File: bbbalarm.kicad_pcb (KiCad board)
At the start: 2 copper layers, 54.6 x 86.4 mm, 34 parts, among them J101 IN0, J102 PWR, J103 IN1, J104 PIR0, J105 PIR1, P8 BeagleBone_Black_Header, P9 BeagleBone_Black_Header, SW101 Reset, SW102 PWR, U101 HCPL-263N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

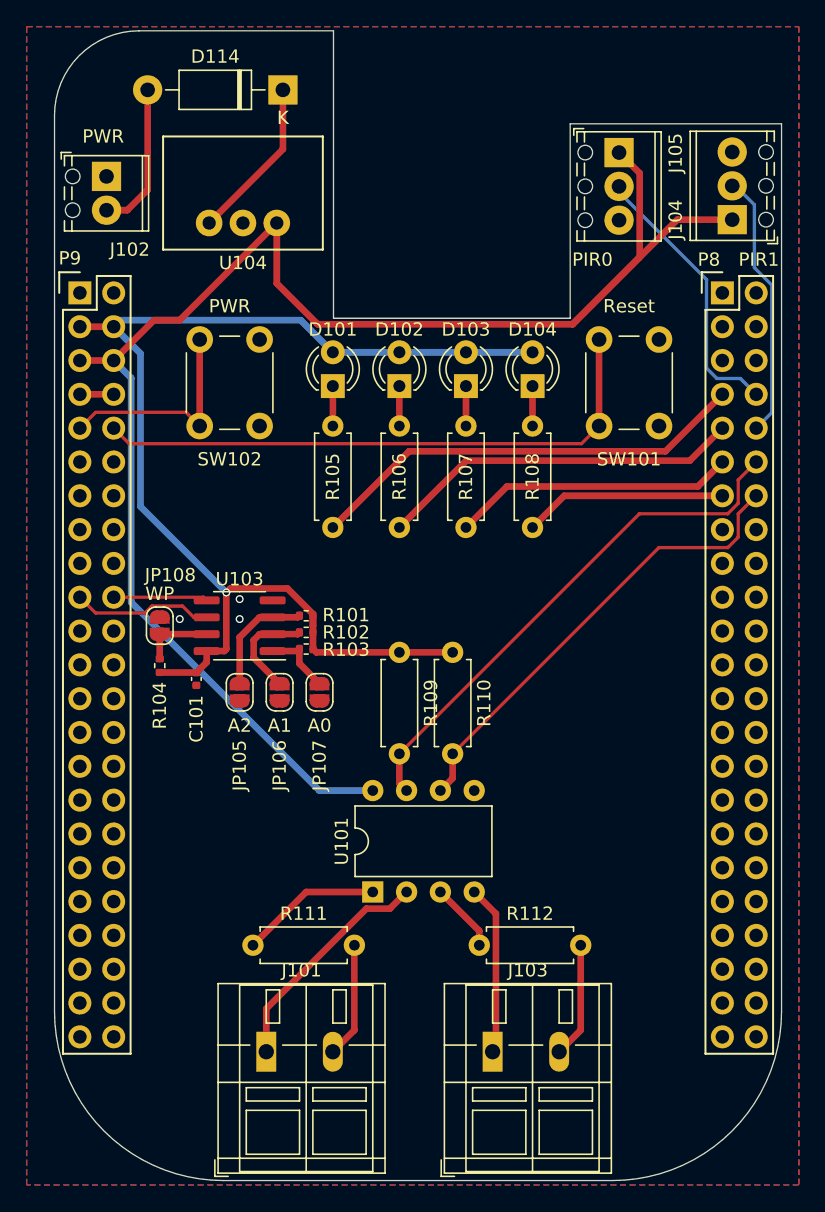
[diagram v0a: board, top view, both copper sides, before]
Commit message: Update to KiCAD v6
Signed-off-by: Benedikt Spranger <b.spranger@linutronix.de>
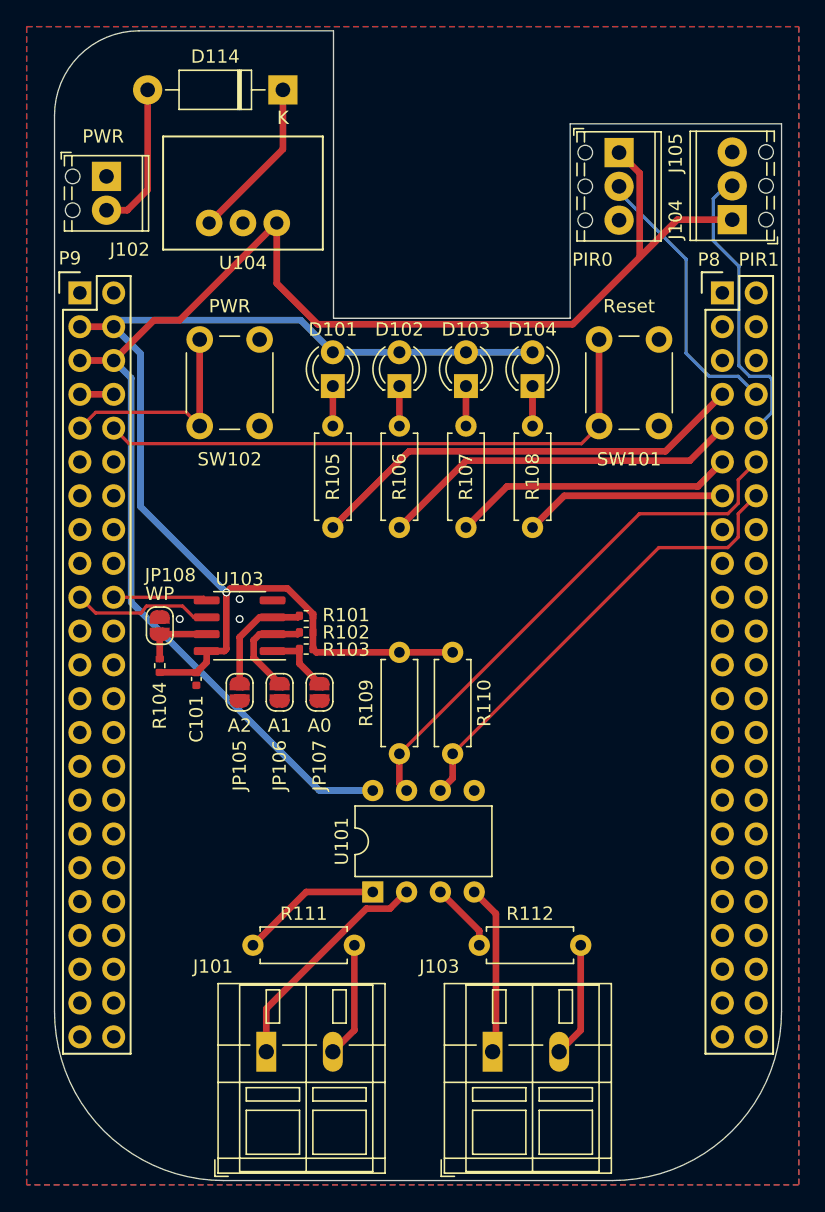
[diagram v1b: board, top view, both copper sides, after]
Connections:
- P8 pad 15: (no net) -> unconnected-(P8-Pad15)
- P8 pad 16: (no net) -> unconnected-(P8-Pad16)
- P8 pad 17: (no net) -> unconnected-(P8-Pad17)
- P8 pad 18: (no net) -> unconnected-(P8-Pad18)
- P8 pad 19: (no net) -> unconnected-(P8-Pad19)
- P8 pad 20: (no net) -> unconnected-(P8-Pad20)
- P8 pad 21: (no net) -> unconnected-(P8-Pad21)
- P8 pad 22: (no net) -> unconnected-(P8-Pad22)
- P8 pad 23: (no net) -> unconnected-(P8-Pad23)
- P8 pad 24: (no net) -> unconnected-(P8-Pad24)
- P8 pad 25: (no net) -> unconnected-(P8-Pad25)
- P8 pad 26: (no net) -> unconnected-(P8-Pad26)
- P8 pad 27: (no net) -> unconnected-(P8-Pad27)
- P8 pad 28: (no net) -> unconnected-(P8-Pad28)
- P8 pad 29: (no net) -> unconnected-(P8-Pad29)
- P8 pad 3: (no net) -> unconnected-(P8-Pad3)
- P8 pad 30: (no net) -> unconnected-(P8-Pad30)
- P8 pad 31: (no net) -> unconnected-(P8-Pad31)
- P8 pad 32: (no net) -> unconnected-(P8-Pad32)
- P8 pad 33: (no net) -> unconnected-(P8-Pad33)
- P8 pad 34: (no net) -> unconnected-(P8-Pad34)
- P8 pad 35: (no net) -> unconnected-(P8-Pad35)
- P8 pad 36: (no net) -> unconnected-(P8-Pad36)
- P8 pad 37: (no net) -> unconnected-(P8-Pad37)
- P8 pad 38: (no net) -> unconnected-(P8-Pad38)
- P8 pad 39: (no net) -> unconnected-(P8-Pad39)
- P8 pad 4: (no net) -> unconnected-(P8-Pad4)
- P8 pad 40: (no net) -> unconnected-(P8-Pad40)
- P8 pad 41: (no net) -> unconnected-(P8-Pad41)
- P8 pad 42: (no net) -> unconnected-(P8-Pad42)
- P8 pad 43: (no net) -> unconnected-(P8-Pad43)
- P8 pad 44: (no net) -> unconnected-(P8-Pad44)
- P8 pad 45: (no net) -> unconnected-(P8-Pad45)
- P8 pad 46: (no net) -> unconnected-(P8-Pad46)
- P8 pad 5: (no net) -> unconnected-(P8-Pad5)
- P8 pad 6: (no net) -> unconnected-(P8-Pad6)
- P9 pad 11: (no net) -> unconnected-(P9-Pad11)
- P9 pad 12: (no net) -> unconnected-(P9-Pad12)
- P9 pad 13: (no net) -> unconnected-(P9-Pad13)
- P9 pad 14: (no net) -> unconnected-(P9-Pad14)
- P9 pad 15: (no net) -> unconnected-(P9-Pad15)
- P9 pad 16: (no net) -> unconnected-(P9-Pad16)
- P9 pad 17: (no net) -> unconnected-(P9-Pad17)
- P9 pad 18: (no net) -> unconnected-(P9-Pad18)
- P9 pad 21: (no net) -> unconnected-(P9-Pad21)
- P9 pad 22: (no net) -> unconnected-(P9-Pad22)
- P9 pad 23: (no net) -> unconnected-(P9-Pad23)
- P9 pad 24: (no net) -> unconnected-(P9-Pad24)
- P9 pad 25: (no net) -> unconnected-(P9-Pad25)
- P9 pad 26: (no net) -> unconnected-(P9-Pad26)
- P9 pad 27: (no net) -> unconnected-(P9-Pad27)
- P9 pad 28: (no net) -> unconnected-(P9-Pad28)
- P9 pad 29: (no net) -> unconnected-(P9-Pad29)
- P9 pad 30: (no net) -> unconnected-(P9-Pad30)
- P9 pad 31: (no net) -> unconnected-(P9-Pad31)
- P9 pad 32: (no net) -> VDD_ADC
- P9 pad 33: (no net) -> unconnected-(P9-Pad33)
- P9 pad 34: (no net) -> GNDA_ADC
- P9 pad 35: (no net) -> unconnected-(P9-Pad35)
- P9 pad 36: (no net) -> unconnected-(P9-Pad36)
- P9 pad 37: (no net) -> unconnected-(P9-Pad37)
- P9 pad 38: (no net) -> unconnected-(P9-Pad38)
- P9 pad 39: (no net) -> unconnected-(P9-Pad39)
- P9 pad 40: (no net) -> unconnected-(P9-Pad40)
- P9 pad 41: (no net) -> unconnected-(P9-Pad41)
- P9 pad 42: (no net) -> unconnected-(P9-Pad42)
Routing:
- net +5V: track 120.7 -> 113.6 mm
- net /PIR1: track 20.1 -> 22.2 mm
- net +3V3: track 90.5 -> 89.8 mm
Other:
- outline, holes or cut-outs redrawn
- net class Default removed

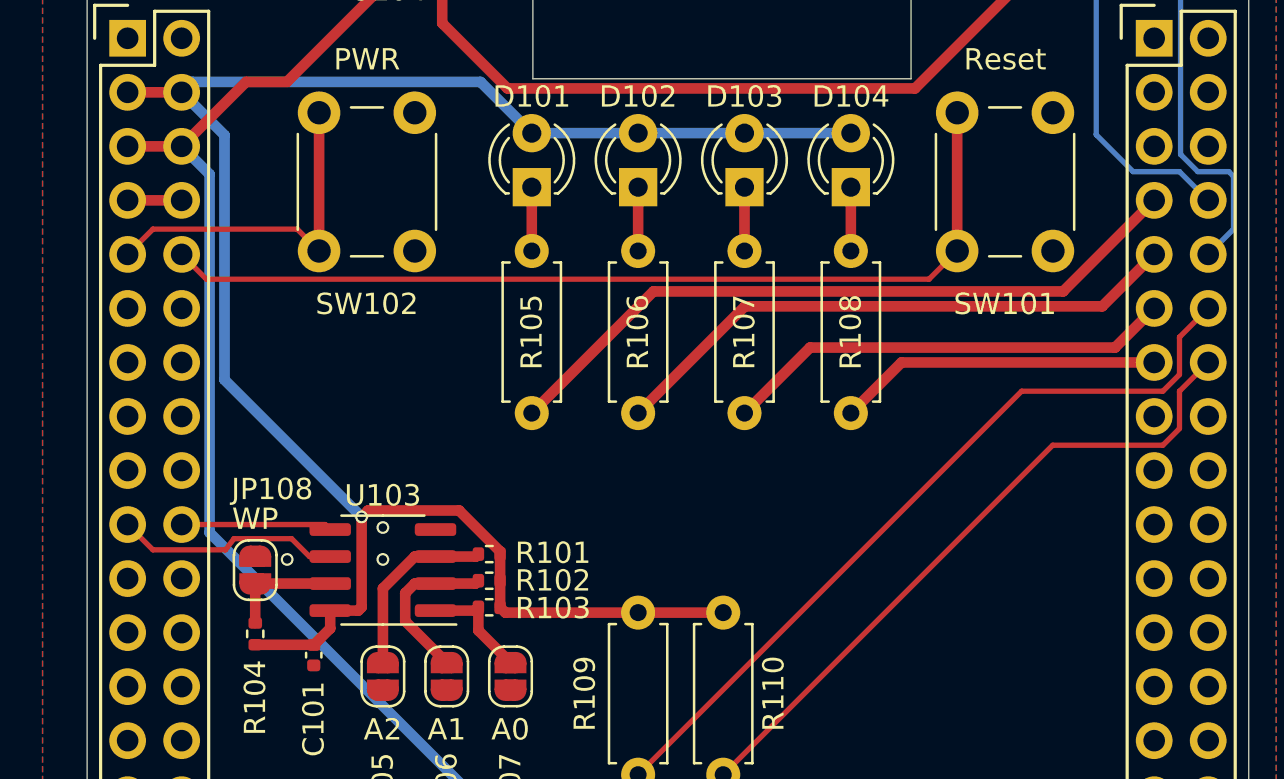
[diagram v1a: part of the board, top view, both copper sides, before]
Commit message: Add Temp sensor and serial header
Signed-off-by: Benedikt Spranger <b.spranger@linutronix.de>
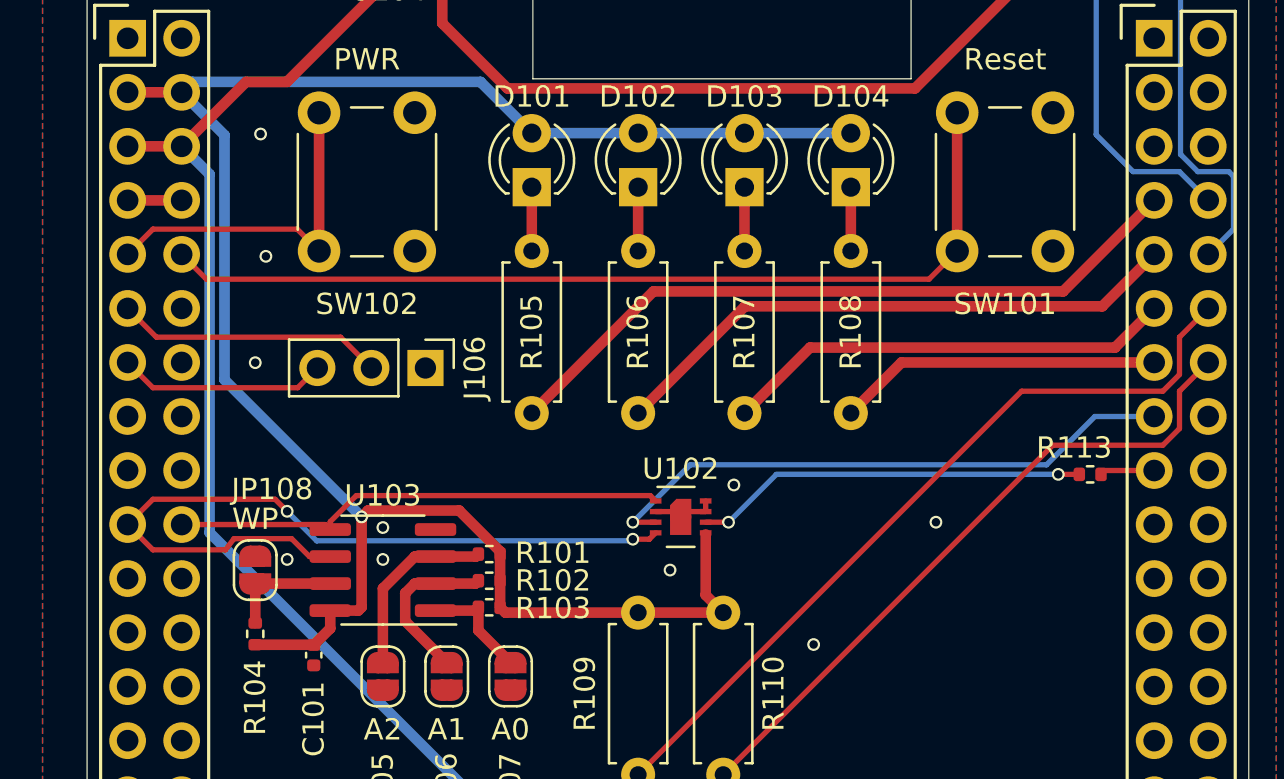
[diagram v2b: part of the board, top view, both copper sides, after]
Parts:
- added J106: serial, Connector_PinHeader_2.54mm:PinHeader_1x03_P2.54mm_Vertical, F.Cu at (130.4, 77.9)
- added R113: 1k, Resistor_SMD:R_0402_1005Metric, F.Cu at (161.6, 82.9)
- added U102: SHT35-DIS, Sensor_Humidity:Sensirion_DFN-8-1EP_2.5x2.5mm_P0.5mm_EP1.1x1.7mm, F.Cu at (142.4, 84.9)
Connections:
- P8 pad 15: unconnected-(P8-Pad15) -> /ALERT
- P8 pad 17: unconnected-(P8-Pad17) -> /nRST
- P9 pad 11: unconnected-(P9-Pad11) -> /RX
- P9 pad 13: unconnected-(P9-Pad13) -> /TX
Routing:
- net /ALERT: track 0.00 -> 27.6 mm, vias 0 -> 1
- net /SCL: track 10.6 -> 36.9 mm, vias 0 -> 2
- net Net-(R113-Pad2): track 0.00 -> 18.5 mm, vias 0 -> 2
- net /SDA: track 7.08 -> 23.4 mm
- net /RX: track 0.00 -> 12.6 mm
- net /TX: track 0.00 -> 9.80 mm
- net +3V3: track 89.8 -> 93.8 mm
- net GNDD: track 0.07 -> 3.13 mm, vias 3 -> 10
- net /nRST: track 0.00 -> 2.57 mm
